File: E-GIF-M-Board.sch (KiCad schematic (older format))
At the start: 0 parts

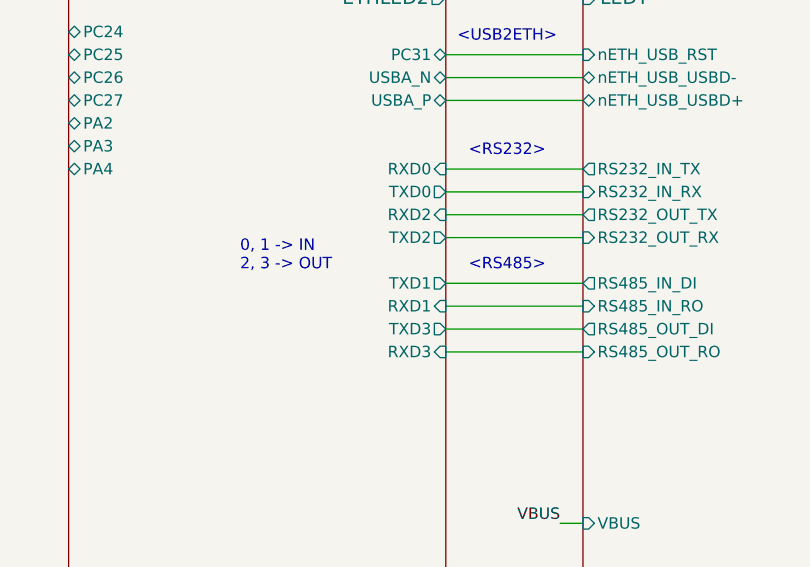
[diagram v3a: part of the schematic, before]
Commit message: Finished first version of PCB.
Modified RJ45 footprint.
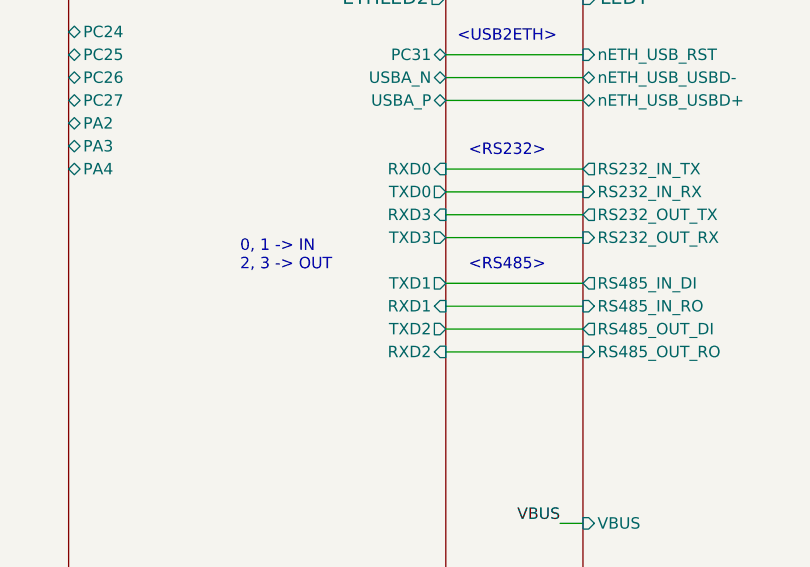
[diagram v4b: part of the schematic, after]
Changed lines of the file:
@@
 F15 "ETHLED1" O R 7300 3000 60
 F16 "ETHLED2" O R 7300 3100 60
-F17 "RXD2" I R 7300 4050 50
+F17 "RXD2" I R 7300 4650 50
 F18 "RXD1" I R 7300 4450 50
 F19 "RXD0" I R 7300 3850 50
-F20 "RXD3" I R 7300 4650 50
-F25 "TXD1" O R 7300 4350 50
-F26 "TXD3" O R 7300 4550 50
-F27 "TXD0" O R 7300 3950 50
-F28 "TXD2" O R 7300 4150 50
-F29 "USBA_N" B R 7300 3450 50
-F30 "USBA_P" B R 7300 3550 50
-F31 "PA4" B L 5650 3850 50
-F32 "PC24" B L 5650 3250 50
-F33 "PC25" B L 5650 3350 50
-F34 "PC26" B L 5650 3450 50
-F35 "PC27" B L 5650 3550 50
-F36 "PA2" B L 5650 3650 50
-F37 "PA3" B L 5650 3750 50
-F38 "PC31" B R 7300 3350 50
+F20 "RXD3" I R 7300 4050 50
+F21 "TXD1" O R 7300 4350 50
+F22 "TXD3" O R 7300 4150 50
+F23 "TXD0" O R 7300 3950 50
+F24 "TXD2" O R 7300 4550 50
+F25 "USBA_N" B R 7300 3450 50
+F26 "USBA_P" B R 7300 3550 50
+F27 "PA4" B L 5650 3850 50
+F28 "PC24" B L 5650 3250 50
+F29 "PC25" B L 5650 3350 50
+F30 "PC26" B L 5650 3450 50
+F31 "PC27" B L 5650 3550 50
+F32 "PA2" B L 5650 3650 50
+F33 "PA3" B L 5650 3750 50
+F34 "PC31" B R 7300 3350 50
 $EndSheet
 $Sheet

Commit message: Modified schematic. v1.1
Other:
- note added: "+RTS"
- note added: "<- Pentru RS232, TX la TX"
- note removed: "0, 1 -> IN\n2, 3 -> OUT"
- note removed: "<- Pentru RS232, RX la TX"
- note removed: "<RS232>"
- note removed: "<RS485>"
- note removed: "<USB2ETH>"

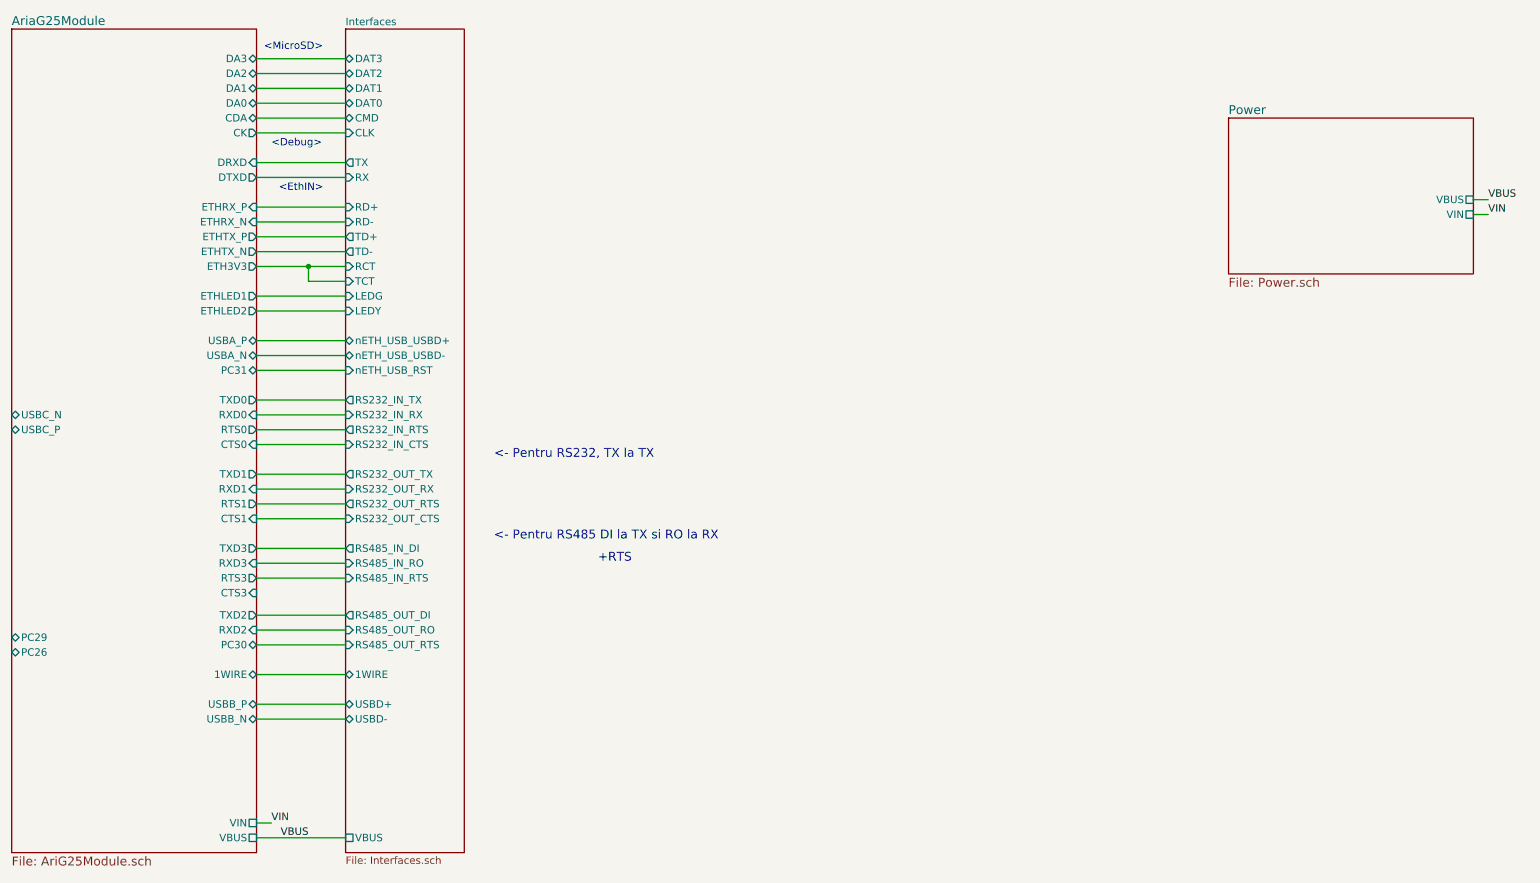
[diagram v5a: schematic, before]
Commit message: Modified board. v1.1 to reflect the schematic change.
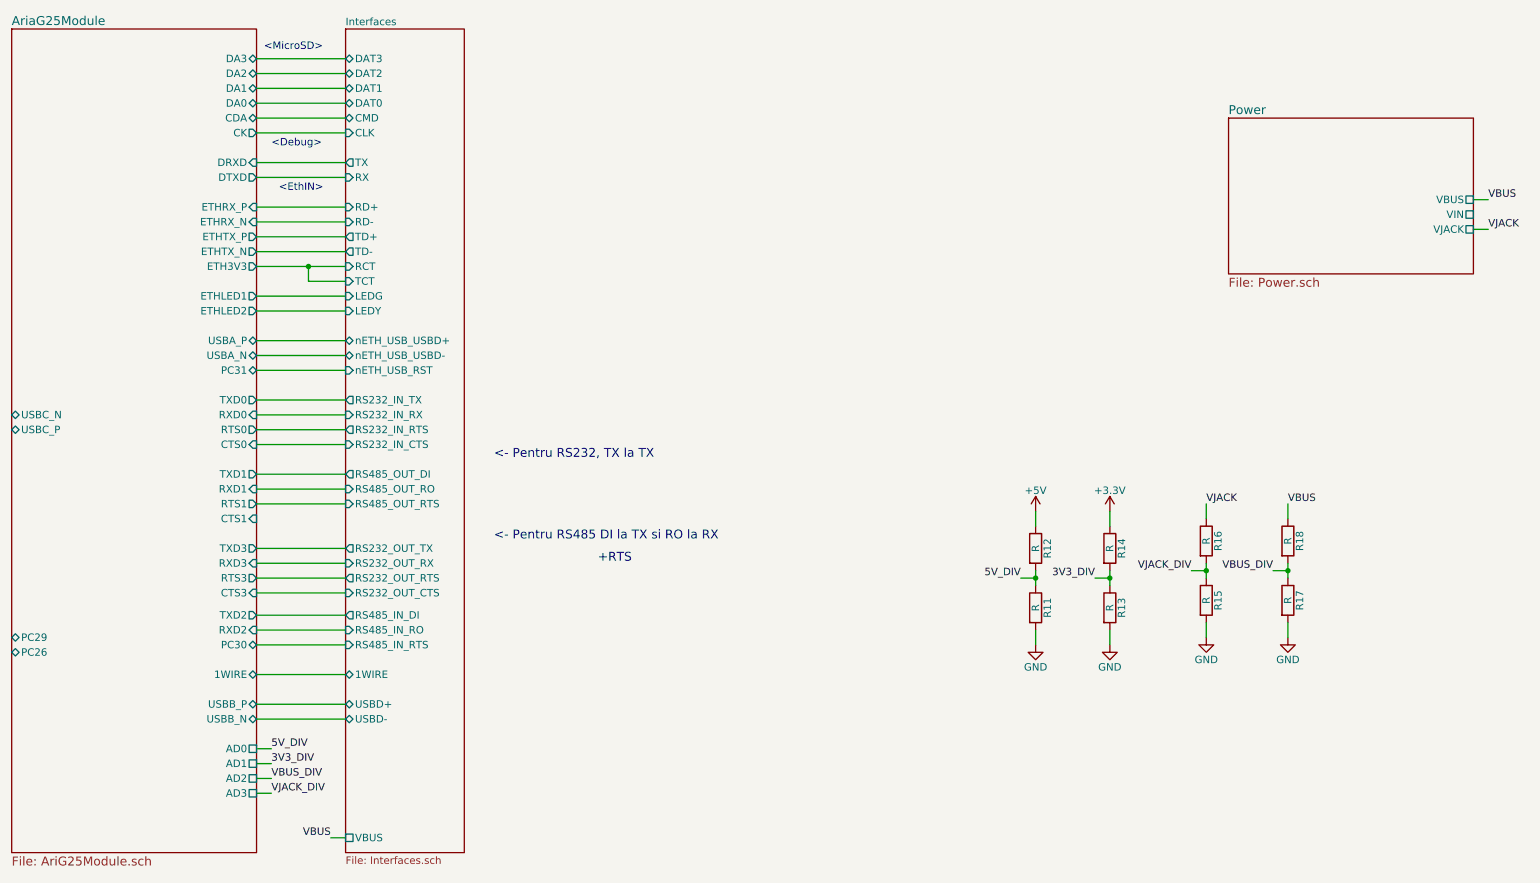
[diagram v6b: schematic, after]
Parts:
- added R11, R12, R13, R14, R15, R16, R17, R18: R, symbol R
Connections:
- net VBUS: now also R18.1
- new net +3V3: R14.1
- new net +5V: R12.1
- new net 3V3_DIV: R13.1, R14.2
- new net 5V_DIV: R11.1, R12.2
- new net GND: R11.2, R13.2, R15.2, R17.2
- new net VBUS_DIV: R17.1, R18.2
- new net VJACK: R16.1
- new net VJACK_DIV: R15.1, R16.2
